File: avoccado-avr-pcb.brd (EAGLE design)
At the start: 17.8 x 33 mm, 24 parts, among them IC1 MCP1703CB, Q1 #MHz, Q2 MOSFET-NCHANNEL2N7002PW, U1 ATMEGA168#, U2 MCP73831, X1 Micro USB

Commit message: add n-chan LL mosfet for vibrator
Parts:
- added R5: 1M, SparkFun-Passives:0805
- R1: value (none) -> 1K
- moved R4 12.5 mm to (16.5, 39.4)
- moved C4 9.16 mm to (8.89, 35.6)
- moved U2 9.16 mm to (12.7, 35.6)
- moved Q2 8.89 mm to (16.5, 35.6)
- moved C19 7.62 mm to (21.1, 24.1)
- moved D1 5.39 mm to (14.0, 39.4), turned to 90 degrees
- moved R3 1.27 mm to (20.3, 29.2)
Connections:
- removed net D5: JP7.5, U1.9
- new net D5-VIBR: JP7.5, R1.1, U1.9
- new net N$6: Q2.1, R1.2, R5.2
- net GND: now also Q2.2, R5.1
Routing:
- net D5-VIBR: track 0.00 -> 3.22 mm
- net D5: track 3.22 -> 0.00 mm
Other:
- board text removed: "Released under the Creative Commons Attribution Share-Alike 3.0 License"
- board text removed: "http://creativecommons.org/licenses/by-sa/3.0"

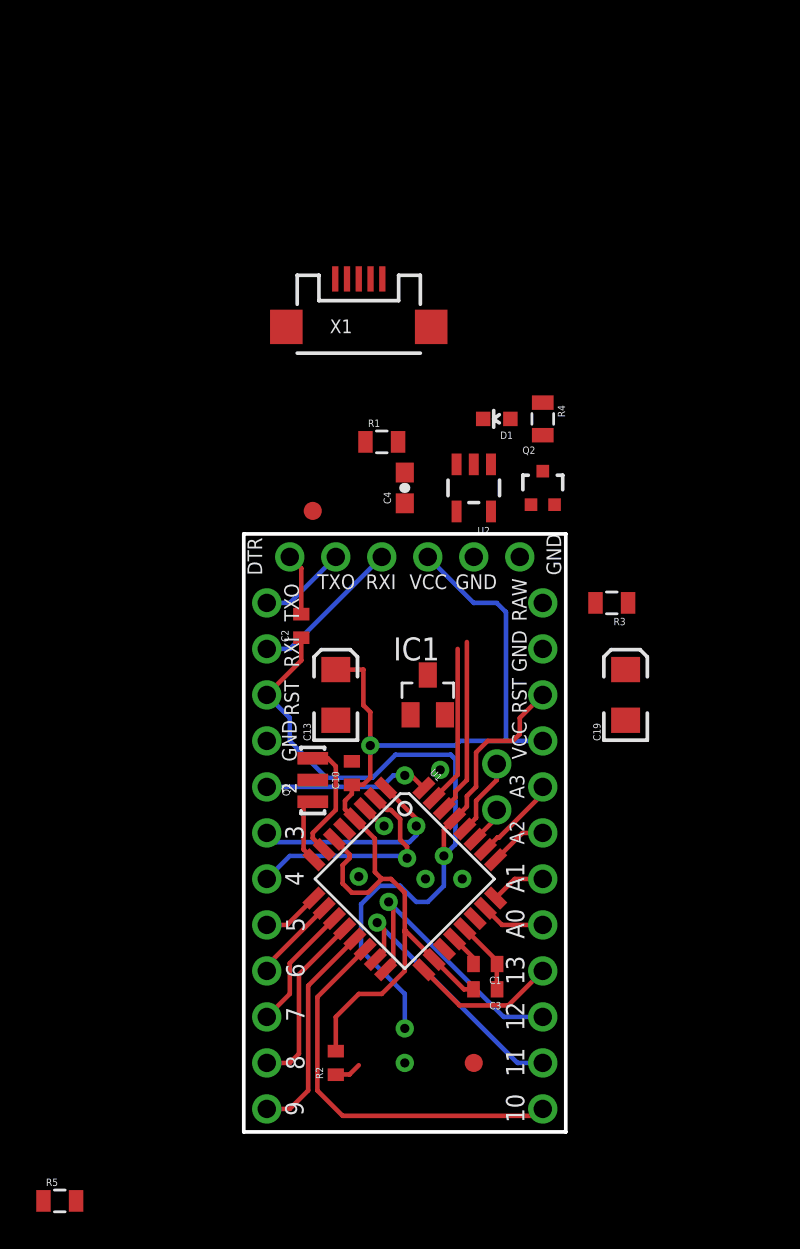
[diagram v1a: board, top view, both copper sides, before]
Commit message: add A6 and A7 analog inputs
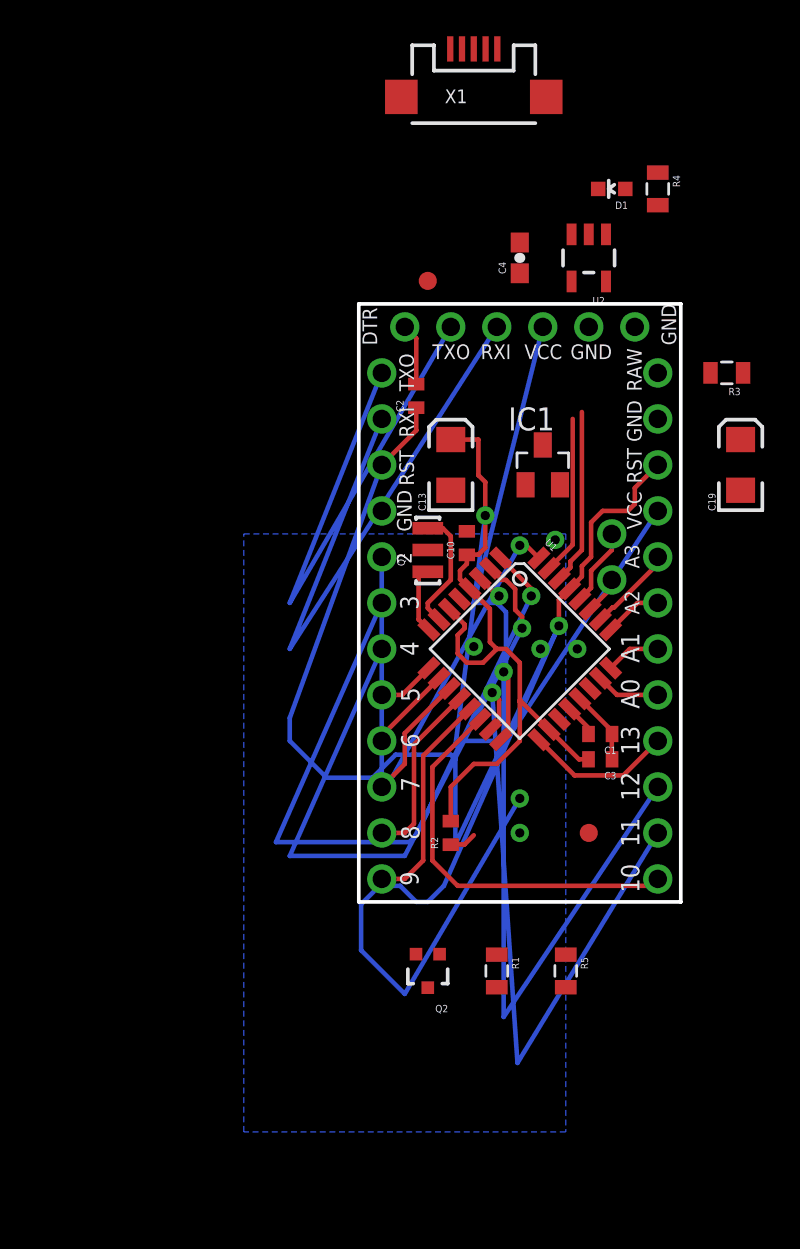
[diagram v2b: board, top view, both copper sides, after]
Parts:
- moved R5 30.7 mm to (17.8, 8.89), turned to 270 degrees
- moved R1 29.9 mm to (14.0, 8.89), turned to 270 degrees
- moved Q2 27.4 mm to (10.2, 8.89), turned to 180 degrees
- moved JP1 14.2 mm to (8.89, 44.5)
- moved JP7 14.2 mm to (7.62, 14.0)
- moved R2 14.2 mm to (11.4, 16.5)
- moved U$2 14.2 mm to (19.1, 16.5)
- moved U1 14.2 mm to (15.2, 26.7)
- moved C3 14.2 mm to (19.7, 20.6)
- moved D1 14.2 mm to (20.3, 52.1)
- moved R4 14.2 mm to (22.9, 52.1)
- moved U$4 14.2 mm to (10.2, 47.0)
- moved C10 14.2 mm to (12.3, 32.5)
- moved C13 14.2 mm to (11.4, 36.8)
- moved C2 14.2 mm to (9.53, 40.6)
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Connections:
- new net A6: U1.19
- new net A7: U1.22
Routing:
- net RESET: track 51.9 -> 102.1 mm
- net VCC: track 61.1 -> 94.5 mm
- net D3: track 11.9 -> 39.8 mm
- net TXO: track 13.7 -> 40.1 mm
- net RXI: track 18.2 -> 44.5 mm
- net D4: track 12.5 -> 37.2 mm
- net MISO: track 15.2 -> 38.4 mm
- net MOSI: track 14.7 -> 37.8 mm
- net D2: track 9.23 -> 29.4 mm

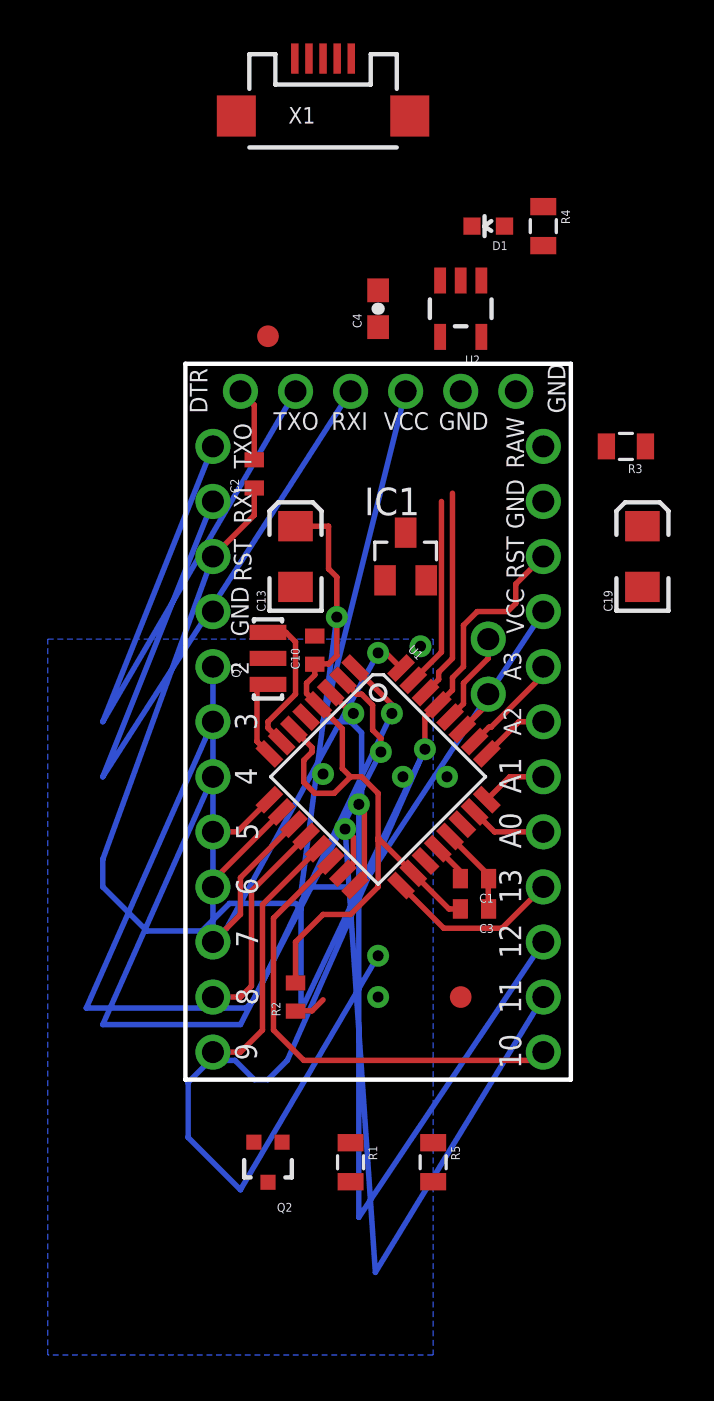
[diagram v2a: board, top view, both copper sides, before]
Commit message: fix fragmented move
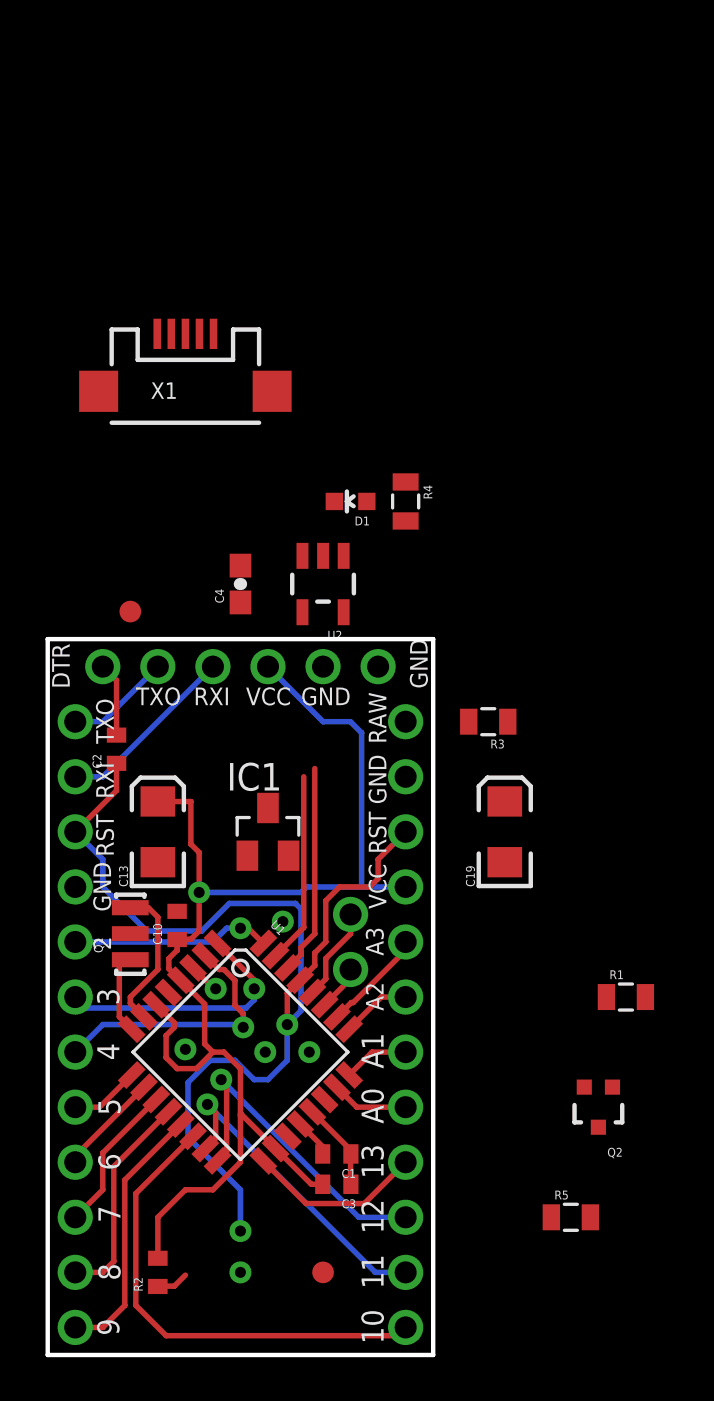
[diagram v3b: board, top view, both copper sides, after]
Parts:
- moved Q2 15.5 mm to (25.4, 11.4)
- moved R1 14.8 mm to (26.7, 16.5), turned to 0 degrees
- moved JP1 14.2 mm to (2.54, 31.8)
- moved JP7 14.2 mm to (1.27, 1.27)
- moved R2 14.2 mm to (5.08, 3.81)
- moved U$2 14.2 mm to (12.7, 3.81)
- moved U1 14.2 mm to (8.89, 14.0)
- moved C3 14.2 mm to (13.3, 7.87)
- moved D1 14.2 mm to (14.0, 39.4)
- moved R4 14.2 mm to (16.5, 39.4)
- moved U$4 14.2 mm to (3.81, 34.3)
- moved C10 14.2 mm to (5.97, 19.8)
- moved C13 14.2 mm to (5.08, 24.1)
- moved C2 14.2 mm to (3.17, 27.9)
- moved IC1 14.2 mm to (10.2, 24.1)
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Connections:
- removed net A6: U1.19
- removed net A7: U1.22
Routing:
- net RESET: track 102.1 -> 51.9 mm
- net VCC: track 94.5 -> 61.1 mm
- net D3: track 39.8 -> 11.9 mm
- net TXO: track 40.1 -> 13.7 mm
- net RXI: track 44.5 -> 18.2 mm
- net D4: track 37.2 -> 12.5 mm
- net MISO: track 38.4 -> 15.2 mm
- net MOSI: track 37.8 -> 14.7 mm
- net D2: track 29.4 -> 9.23 mm

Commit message: m
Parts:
- D1: value RED -> CHARGE LED
- moved Q2 16.1 mm to (10.2, 6.35)
- moved C13 14.5 mm to (14.0, 35.6)
- moved C19 14.5 mm to (30.0, 35.6)
- moved IC1 14.5 mm to (19.1, 35.6)
- moved C1 14.5 mm to (22.2, 20.7)
- moved C10 14.5 mm to (14.9, 31.2)
- moved C3 14.5 mm to (22.2, 19.3)
- moved C4 14.5 mm to (17.8, 47.0)
- moved D1 14.5 mm to (22.9, 50.8)
- moved JP1 14.5 mm to (11.4, 43.2)
- moved JP2 14.5 mm to (22.9, 29.2)
- moved JP7 14.5 mm to (10.2, 12.7)
- moved Q1 14.5 mm to (12.7, 30.9)
- moved R2 14.5 mm to (14.0, 15.2)
- moved R3 14.5 mm to (29.2, 40.6)
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
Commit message: wip change to SMD headers
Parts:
- added JP10, JP17, JP3, JP4, JP5, JP8, JP9: (no value), SparkFun-Connectors:1X04-SMD
- moved JP6 21.6 mm to (47.0, 40.6)
- moved C19 8.52 mm to (22.4, 39.4)
- moved JP7 7.62 mm to (2.54, 12.7)
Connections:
- net A0: now also JP5.1
- net A1: now also JP5.2
- net A2: now also JP5.3
- net A3: now also JP5.4
- net D10: now also JP4.1
- net D2: now also JP10.4
- net D3: now also JP10.3
- net D4: now also JP10.2
- net D5-VIBR: now also JP10.1
- net D6: now also JP17.4
- net D7: now also JP17.3
- net D8: now also JP17.2
- net D9: now also JP17.1
- net GND: now also JP8.3, JP9.1
- net MISO: now also JP4.3
- net MOSI: now also JP4.2
- net RAW: now also JP8.4
- net RESET: now also JP8.2, JP9.2
- net RXI: now also JP9.3
- net SCK: now also JP4.4
- net TXO: now also JP9.4
- net VCC: now also JP8.1
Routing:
- net RESET: track 51.9 -> 64.3 mm
- net D9: track 12.1 -> 19.8 mm
- net D2: track 9.23 -> 16.8 mm
- net D5-VIBR: track 3.22 -> 10.8 mm
- net RXI: track 18.2 -> 25.8 mm
- net D8: track 9.93 -> 17.6 mm
- net TXO: track 13.7 -> 21.3 mm
- net D3: track 11.9 -> 19.4 mm
- net D6: track 4.77 -> 12.1 mm
- net D7: track 6.98 -> 14.2 mm
- net D4: track 12.5 -> 19.7 mm
- net SCK: track 8.17 -> 5.48 mm
- net A0: track 3.55 -> 1.30 mm
- net MISO: track 15.2 -> 13.0 mm
- net VCC: track 61.1 -> 59.0 mm
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
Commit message: evaluating SMD pads
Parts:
- removed JP10, JP17, JP3, JP5, JP8, JP9: (no value), SparkFun-Connectors:1X04-SMD
- JP4: value (none) -> M01SMD-4.5X1.5; device SparkFun-Connectors:1X04-SMD -> SparkFun-Connectors:PAD-1.5X4.5
- moved JP4 28.2 mm to (2.54, 12.7)
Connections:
- net A0: no longer JP5.1
- net A1: no longer JP5.2
- net A2: no longer JP5.3
- net A3: no longer JP5.4
- net D10: no longer JP4.1
- net D2: no longer JP10.4
- net D3: no longer JP10.3
- net D4: no longer JP10.2
- net D5-VIBR: no longer JP10.1
- net D6: no longer JP17.4
- net D7: no longer JP17.3
- net D8: no longer JP17.2
- net D9: no longer JP17.1
- net GND: no longer JP8.3, JP9.1
- net MISO: no longer JP4.3
- net MOSI: no longer JP4.2
- net RAW: no longer JP8.4
- net RESET: no longer JP8.2, JP9.2
- net RXI: no longer JP9.3
- net SCK: no longer JP4.4
- net TXO: no longer JP9.4
- net VCC: no longer JP8.1

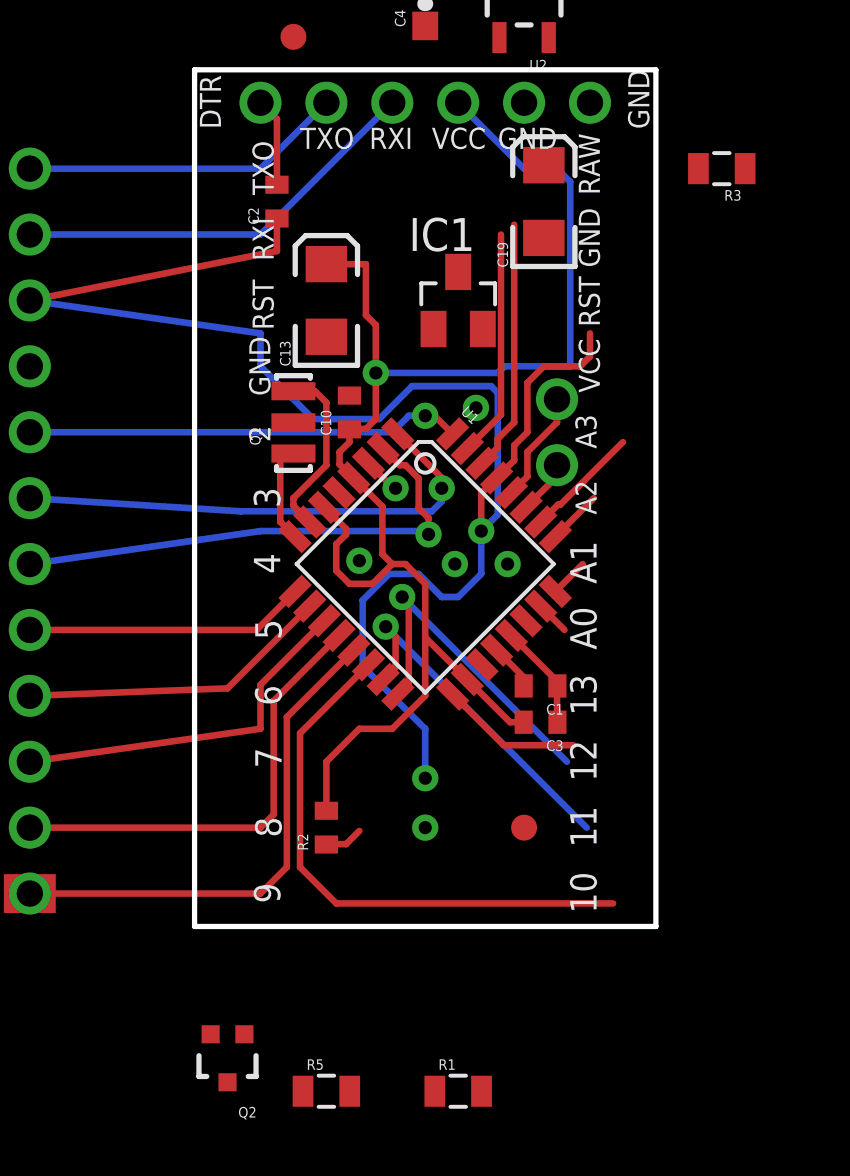
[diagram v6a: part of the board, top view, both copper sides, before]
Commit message: exchanged THT pin rows for custom SMD pads
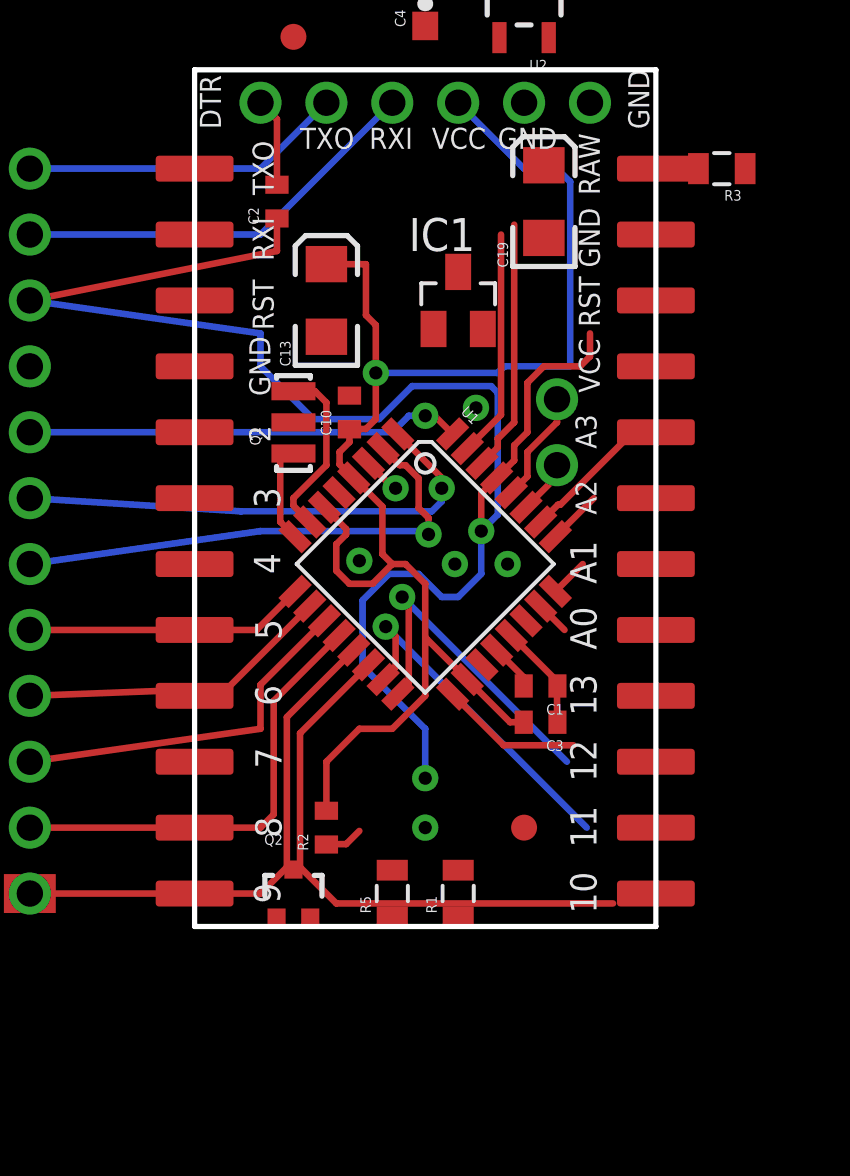
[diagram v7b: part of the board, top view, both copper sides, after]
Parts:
- added JP10, JP11, JP3, JP5, JP8, JP9: (no value), smd-pads:1X04-SMD
- moved R5 8.03 mm to (16.5, 12.7), turned to 90 degrees
- moved R1 7.62 mm to (19.1, 12.7), turned to 90 degrees
- moved Q2 6.84 mm to (12.7, 12.7), turned to 0 degrees
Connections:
- net A0: now also JP5.4
- net A1: now also JP5.3
- net A2: now also JP5.2
- net A3: now also JP5.1
- net D10: now also JP8.4
- net D2: now also JP10.4
- net D3: now also JP10.3
- net D4: now also JP10.2
- net D5-VIBR: now also JP10.1
- net D6: now also JP9.4
- net D7: now also JP9.3
- net D8: now also JP9.2
- net D9: now also JP9.1
- net GND: now also JP11.1, JP3.2
- net MISO: now also JP8.2
- net MOSI: now also JP8.3
- net RAW: now also JP3.1
- net RESET: now also JP11.2, JP3.3
- net RXI: now also JP11.3
- net SCK: now also JP8.1
- net TXO: now also JP11.4
- net VCC: now also JP3.4
